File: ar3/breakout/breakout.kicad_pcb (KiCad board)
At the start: 2 copper layers, 1 part, among them U1 Teensy3.5

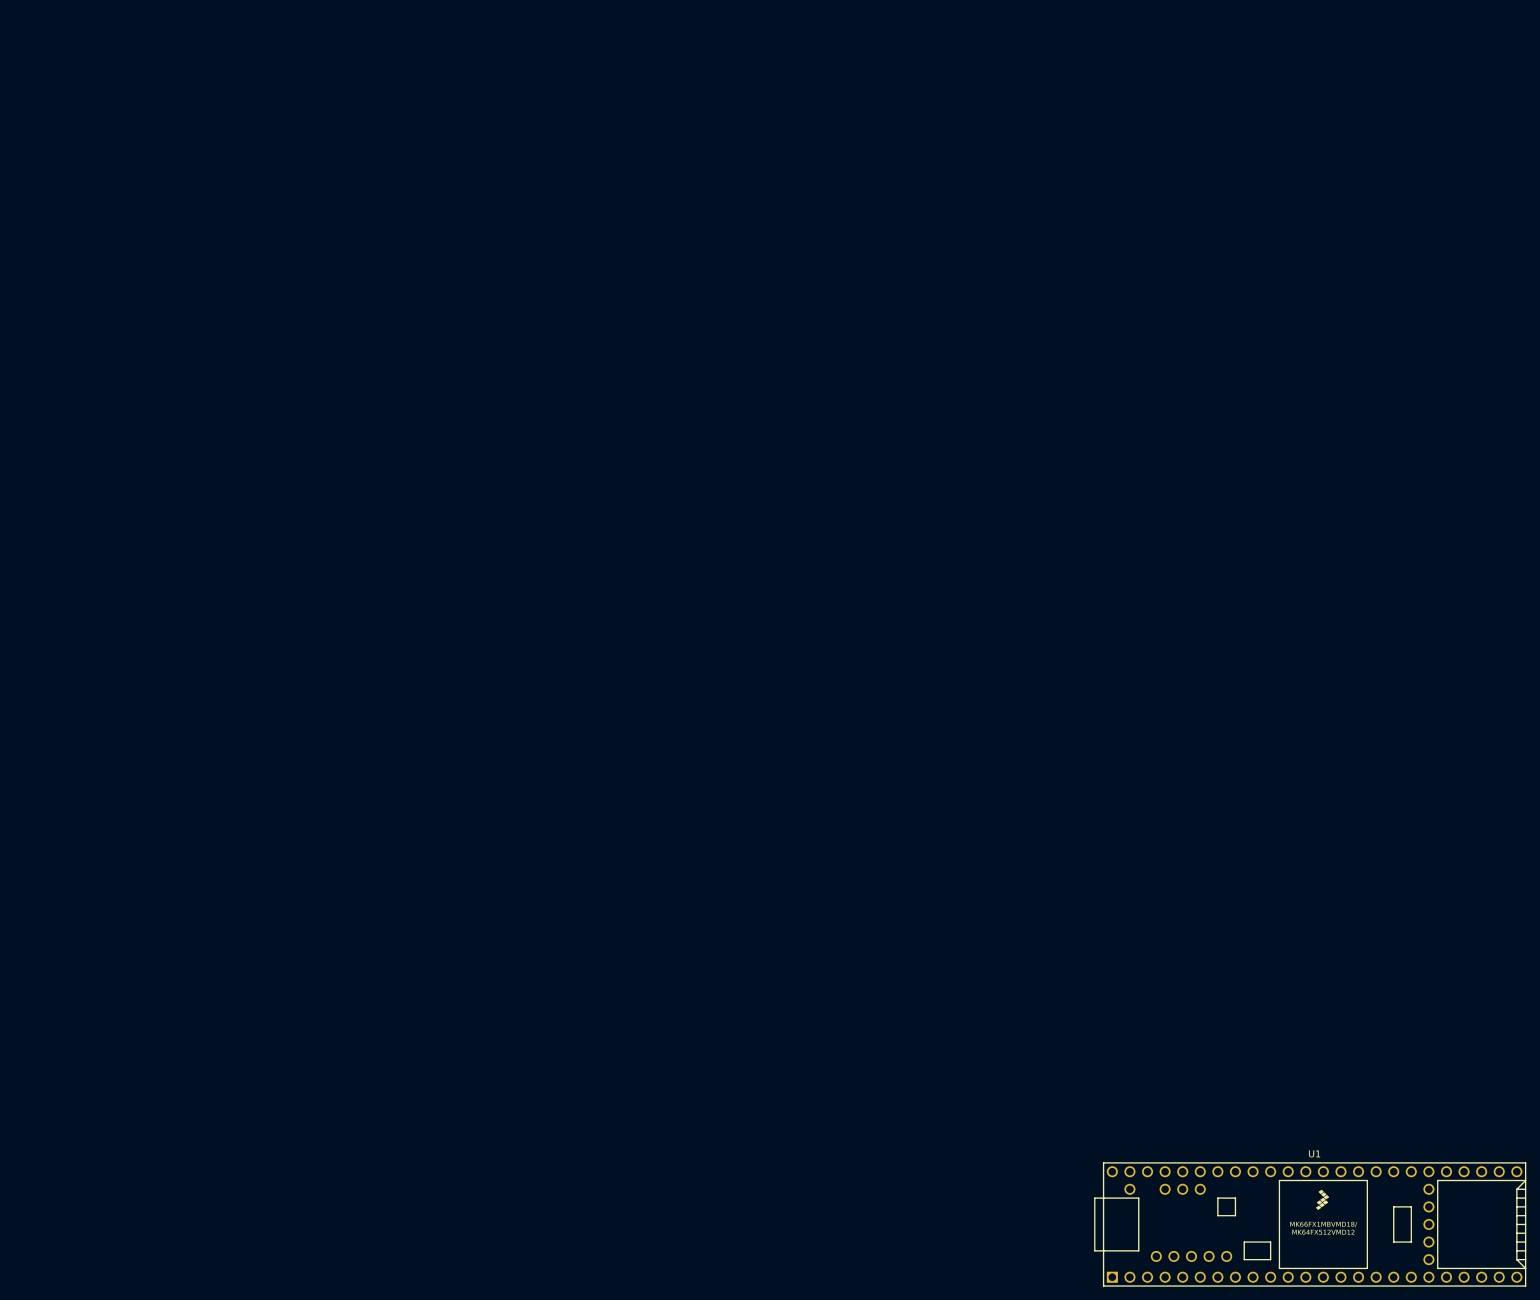
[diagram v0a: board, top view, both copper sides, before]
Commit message: Added v1 gerber files for AR3 controller PCB, plus simple arduino encoder code
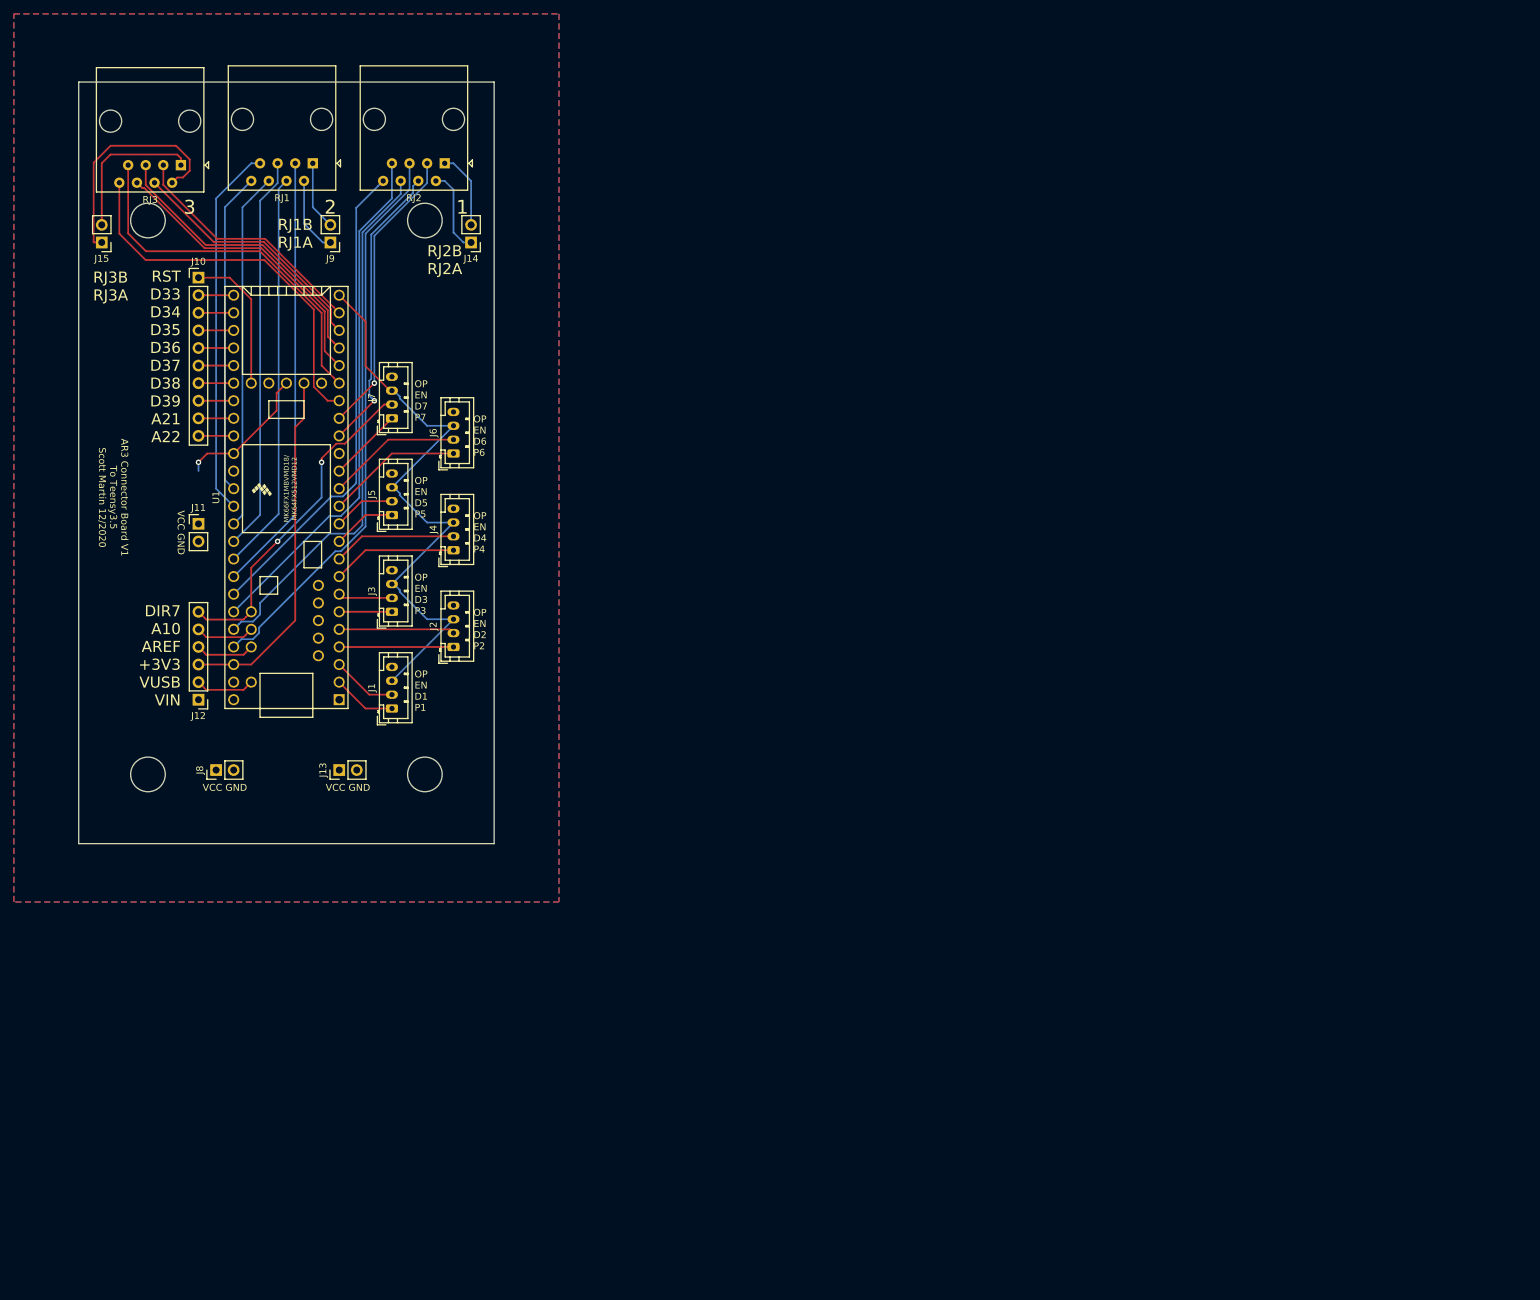
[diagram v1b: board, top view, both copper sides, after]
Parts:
- added J1: Conn_01x04_Male, Connector_JST:JST_PH_B4B-PH-K_1x04_P2.00mm_Vertical, F.Cu at (15.2, 30.5)
- added J10: Conn_01x10_Male, Connector_PinHeader_2.54mm:PinHeader_1x10_P2.54mm_Vertical, F.Cu at (-12.7, -31.8)
- added J11: Conn_01x02_Male, Connector_PinHeader_2.54mm:PinHeader_1x02_P2.54mm_Vertical, F.Cu at (-12.7, 3.81)
- added J12: Conn_01x06_Male, Connector_PinHeader_2.54mm:PinHeader_1x06_P2.54mm_Vertical, F.Cu at (-12.7, 29.2)
- added J13: Conn_01x02_Male, Connector_PinHeader_2.54mm:PinHeader_1x02_P2.54mm_Vertical, F.Cu at (7.62, 39.4)
- added J14: Conn_01x02_Male, Connector_PinHeader_2.54mm:PinHeader_1x02_P2.54mm_Vertical, F.Cu at (26.7, -36.8)
- added J15: Conn_01x02_Male, Connector_PinHeader_2.54mm:PinHeader_1x02_P2.54mm_Vertical, F.Cu at (-26.7, -36.8)
- added J2: Conn_01x04_Male, Connector_JST:JST_PH_B4B-PH-K_1x04_P2.00mm_Vertical, F.Cu at (24.1, 21.6)
- added J3: Conn_01x04_Male, Connector_JST:JST_PH_B4B-PH-K_1x04_P2.00mm_Vertical, F.Cu at (15.2, 16.5)
- added J4: Conn_01x04_Male, Connector_JST:JST_PH_B4B-PH-K_1x04_P2.00mm_Vertical, F.Cu at (24.1, 7.62)
- added J5: Conn_01x04_Male, Connector_JST:JST_PH_B4B-PH-K_1x04_P2.00mm_Vertical, F.Cu at (15.2, 2.54)
- added J6: Conn_01x04_Male, Connector_JST:JST_PH_B4B-PH-K_1x04_P2.00mm_Vertical, F.Cu at (24.1, -6.35)
- added J7: Conn_01x04_Male, Connector_JST:JST_PH_B4B-PH-K_1x04_P2.00mm_Vertical, F.Cu at (15.2, -11.4)
- added J8: Conn_01x02_Male, Connector_PinHeader_2.54mm:PinHeader_1x02_P2.54mm_Vertical, F.Cu at (-10.2, 39.4)
- added J9: Conn_01x02_Male, Connector_PinHeader_2.54mm:PinHeader_1x02_P2.54mm_Vertical, F.Cu at (6.35, -36.8)
- added RJ1: RJ45, Connector_RJ:RJ45_Amphenol_54602-x08_Horizontal, F.Cu at (3.81, -48.3)
- added RJ2: RJ45, Connector_RJ:RJ45_Amphenol_54602-x08_Horizontal, F.Cu at (22.9, -48.3)
- added RJ3: RJ45, Connector_RJ:RJ45_Amphenol_54602-x08_Horizontal, F.Cu at (-15.2, -48.0)
- moved U1 181.9 mm to (0.00, 0.00), turned to 90 degrees
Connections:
- U1 pad 1: (no net) -> GND
- U1 pad 10: (no net) -> /PUL5
- U1 pad 11: (no net) -> /DIR5
- U1 pad 12: (no net) -> /PUL6
- U1 pad 13: (no net) -> /DIR6
- U1 pad 14: (no net) -> /PUL7
- U1 pad 16: (no net) -> /J6A
- U1 pad 17: (no net) -> /J6B
- U1 pad 18: (no net) -> /J1LIM
- U1 pad 19: (no net) -> /J2LIM
- U1 pad 2: (no net) -> /PUL1
- U1 pad 20: (no net) -> /J3LIM
- U1 pad 21: (no net) -> /J4LIM
- U1 pad 22: (no net) -> /J5LIM
- U1 pad 23: (no net) -> /J6LIM
- U1 pad 24: (no net) -> /ENA
- U1 pad 26: (no net) -> +3V3
- U1 pad 27: (no net) -> GND
- U1 pad 29: (no net) -> Net-(J10-Pad1)
- U1 pad 3: (no net) -> /DIR1
- U1 pad 30: (no net) -> Net-(J10-Pad2)
- U1 pad 31: (no net) -> Net-(J10-Pad3)
- U1 pad 32: (no net) -> Net-(J10-Pad4)
- U1 pad 33: (no net) -> Net-(J10-Pad5)
- U1 pad 34: (no net) -> Net-(J10-Pad6)
- U1 pad 35: (no net) -> Net-(J10-Pad7)
- U1 pad 36: (no net) -> Net-(J10-Pad8)
- U1 pad 37: (no net) -> Net-(J10-Pad9)
- U1 pad 38: (no net) -> Net-(J10-Pad10)
- U1 pad 39: (no net) -> GND
- U1 pad 4: (no net) -> /PUL2
- U1 pad 41: (no net) -> /J1A
- U1 pad 42: (no net) -> /J1B
- U1 pad 43: (no net) -> /J2A
- U1 pad 44: (no net) -> /J2B
- U1 pad 45: (no net) -> /J3A
- U1 pad 46: (no net) -> /J3B
- U1 pad 47: (no net) -> /J4A
- U1 pad 48: (no net) -> /J4B
- U1 pad 49: (no net) -> /J5A
- U1 pad 5: (no net) -> /DIR2
- U1 pad 50: (no net) -> /J5B
- U1 pad 51: (no net) -> +3V3
- U1 pad 52: (no net) -> GND
- U1 pad 53: (no net) -> OPTO
- U1 pad 54: (no net) -> Net-(J12-Pad2)
- U1 pad 55: (no net) -> Net-(J12-Pad4)
- U1 pad 56: (no net) -> Net-(J12-Pad5)
- U1 pad 57: (no net) -> /DIR7
- U1 pad 6: (no net) -> /PUL3
- U1 pad 7: (no net) -> /DIR3
- U1 pad 8: (no net) -> /PUL4
- U1 pad 9: (no net) -> /DIR4
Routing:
- net /ENA: track 0.00 -> 88.3 mm
- net /J5B: track 0.00 -> 81.8 mm
- net /J5A: track 0.00 -> 77.8 mm
- net /J4B: track 0.00 -> 75.2 mm
- net /J4A: track 0.00 -> 69.6 mm
- net /J3B: track 0.00 -> 63.4 mm
- net /J3A: track 0.00 -> 57.8 mm
- net /J2B: track 0.00 -> 57.2 mm
- net /J1LIM: track 0.00 -> 55.7 mm
- net /J1B: track 0.00 -> 54.0 mm
- net /J2LIM: track 0.00 -> 53.8 mm
- net /J2A: track 0.00 -> 51.6 mm
- net +3V3: track 0.00 -> 51.4 mm
- net /DIR7: track 0.00 -> 48.3 mm, vias 0 -> 2
- net /J1A: track 0.00 -> 46.6 mm
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- added copper zone on B.Cu, net GND
- added copper zone on F.Cu, net OPTO
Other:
- board outline added: 60 x 110 mm
- board text added: "1"
- board text added: "2"
- board text added: "3"
- board text added: "AR3 Connector Board V1 To Teensy3.5 Scott Martin 12/2020"
- board text added: "DIR7 A10 AREF +3V3 VUSB VIN"
- board text added: "OP EN D1 P1"
- board text added: "OP EN D2 P2"
- board text added: "OP EN D3 P3"
- board text added: "OP EN D4 P4"
- board text added: "OP EN D5 P5"
- board text added: "OP EN D6 P6"
- board text added: "OP EN D7 P7"
- board text added: "RJ1B RJ1A"
- board text added: "RJ2B RJ2A"
- board text added: "RJ3B RJ3A"
- board text added: "RST D33 D34 D35 D36 D37 D38 D39 A21 A22"
- board text added: "VCC GND"

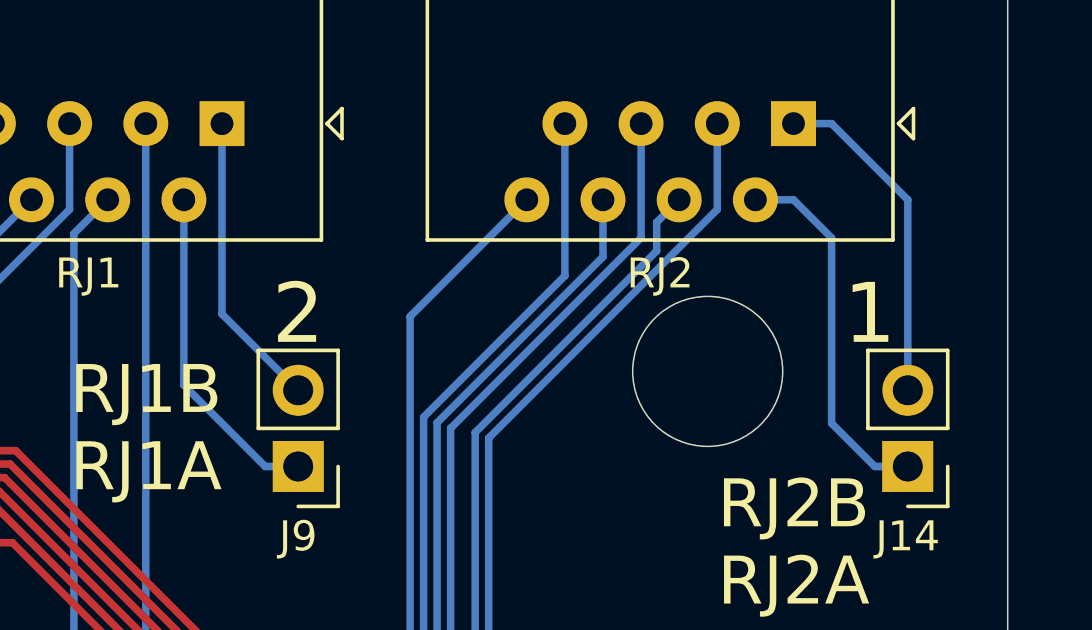
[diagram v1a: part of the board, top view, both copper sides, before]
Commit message: Updated PCB silk for AR3 breakout, worked on AR3 claw URDF file and visualization for it
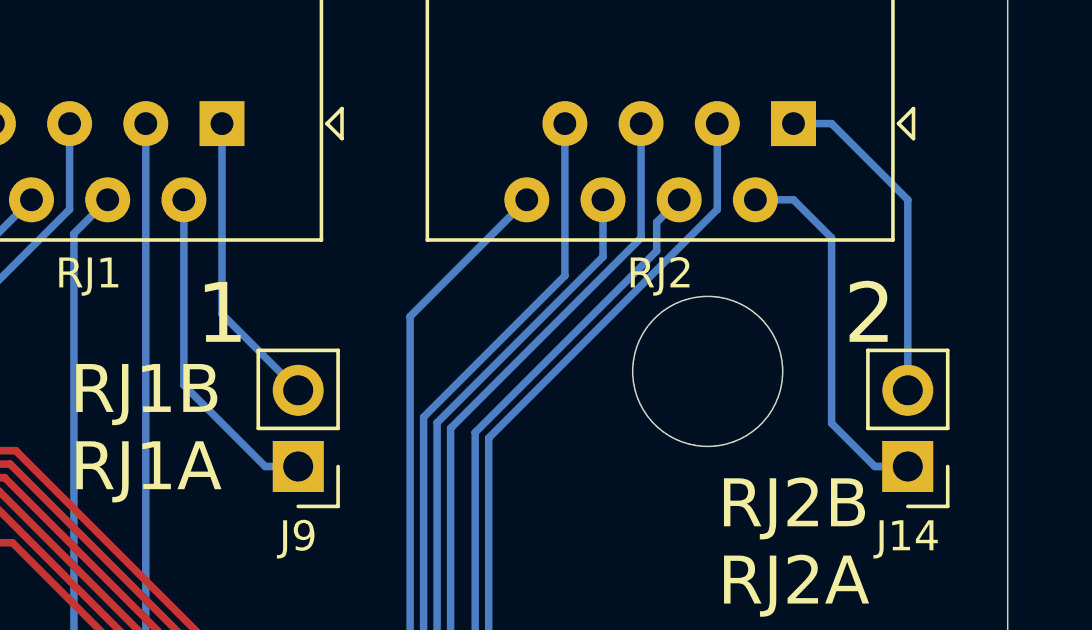
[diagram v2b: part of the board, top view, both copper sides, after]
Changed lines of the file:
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@@
     )
   )
-  (gr_text 1 (at 25.4 -41.91) (layer F.SilkS)
+  (gr_text 1 (at 3.81 -41.91) (layer F.SilkS)
     (effects (font (size 2 2) (thickness 0.15)))
   )
-  (gr_text 2 (at 6.35 -41.91) (layer F.SilkS)
+  (gr_text 2 (at 25.4 -41.91) (layer F.SilkS)
     (effects (font (size 2 2) (thickness 0.15)))
   )
